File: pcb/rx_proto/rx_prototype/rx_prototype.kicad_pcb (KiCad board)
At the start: 10 copper layers, 50 parts, among them U1 nice_nano, U2 MPU-6500, U3 QMC5883P, U4 MCP6004, U5 MCP6004, U6 74HC4051

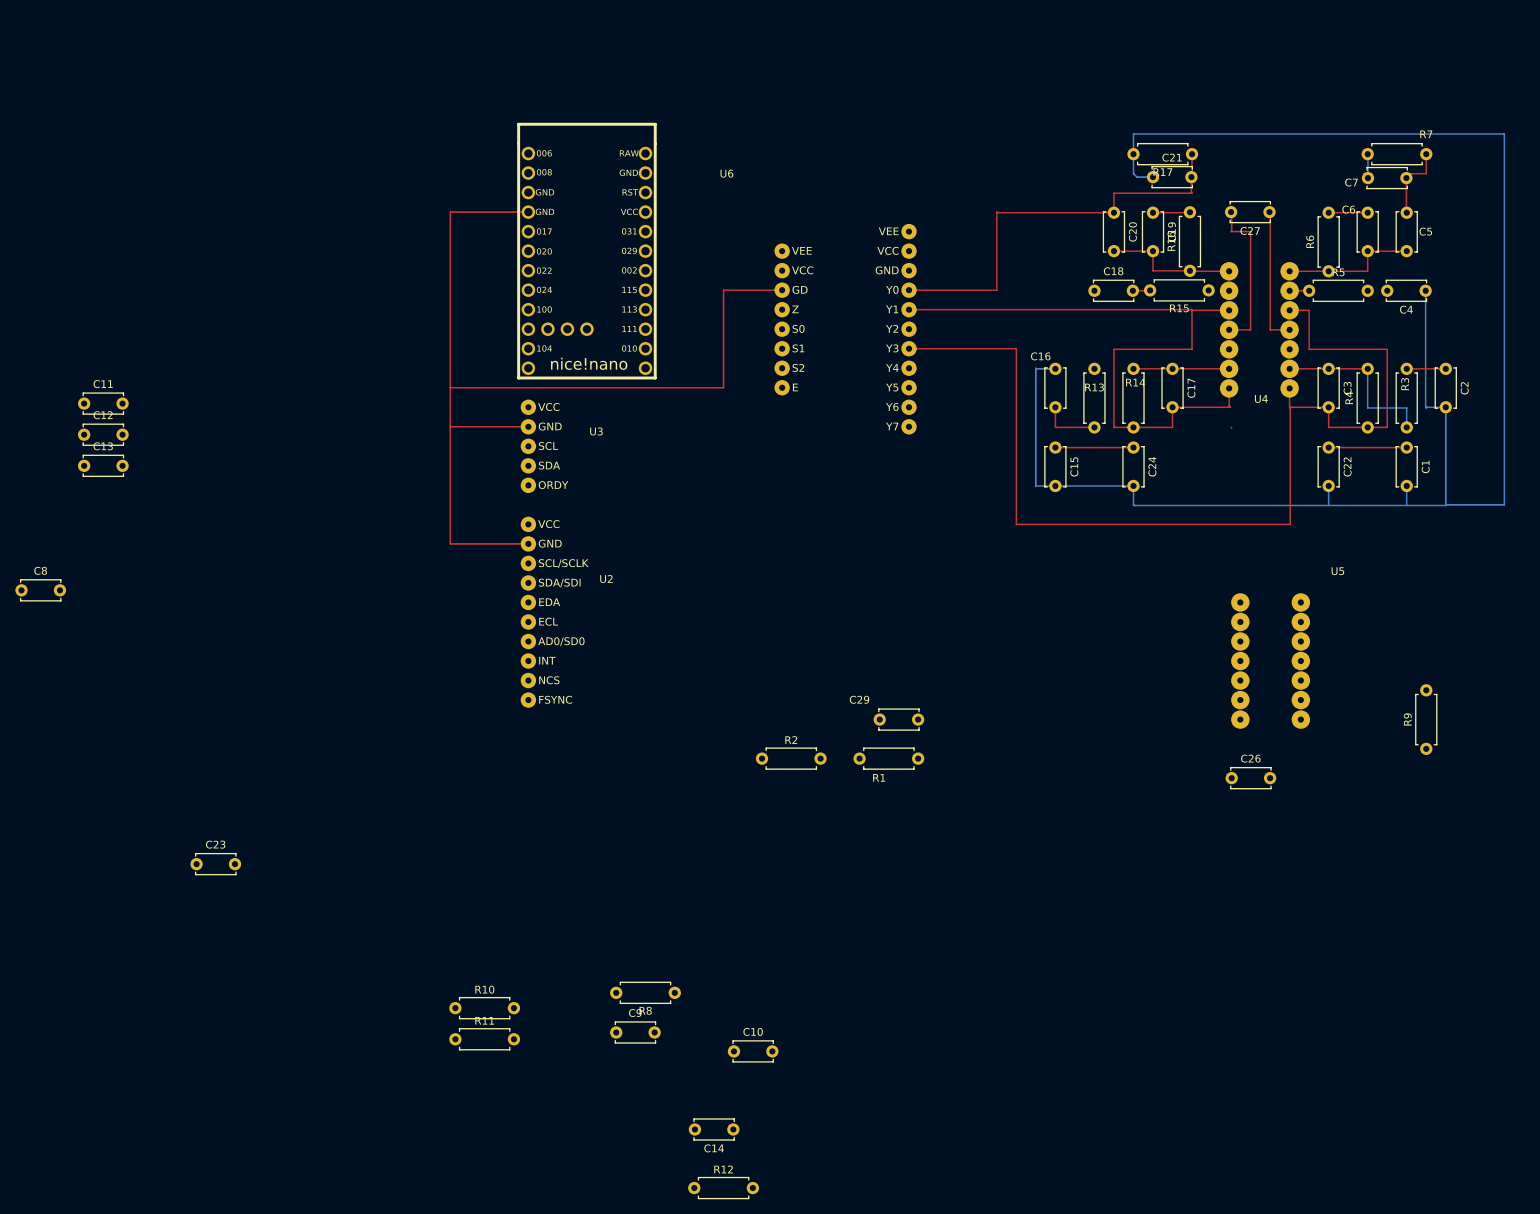
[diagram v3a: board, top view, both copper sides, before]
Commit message: Completed perboard prototype
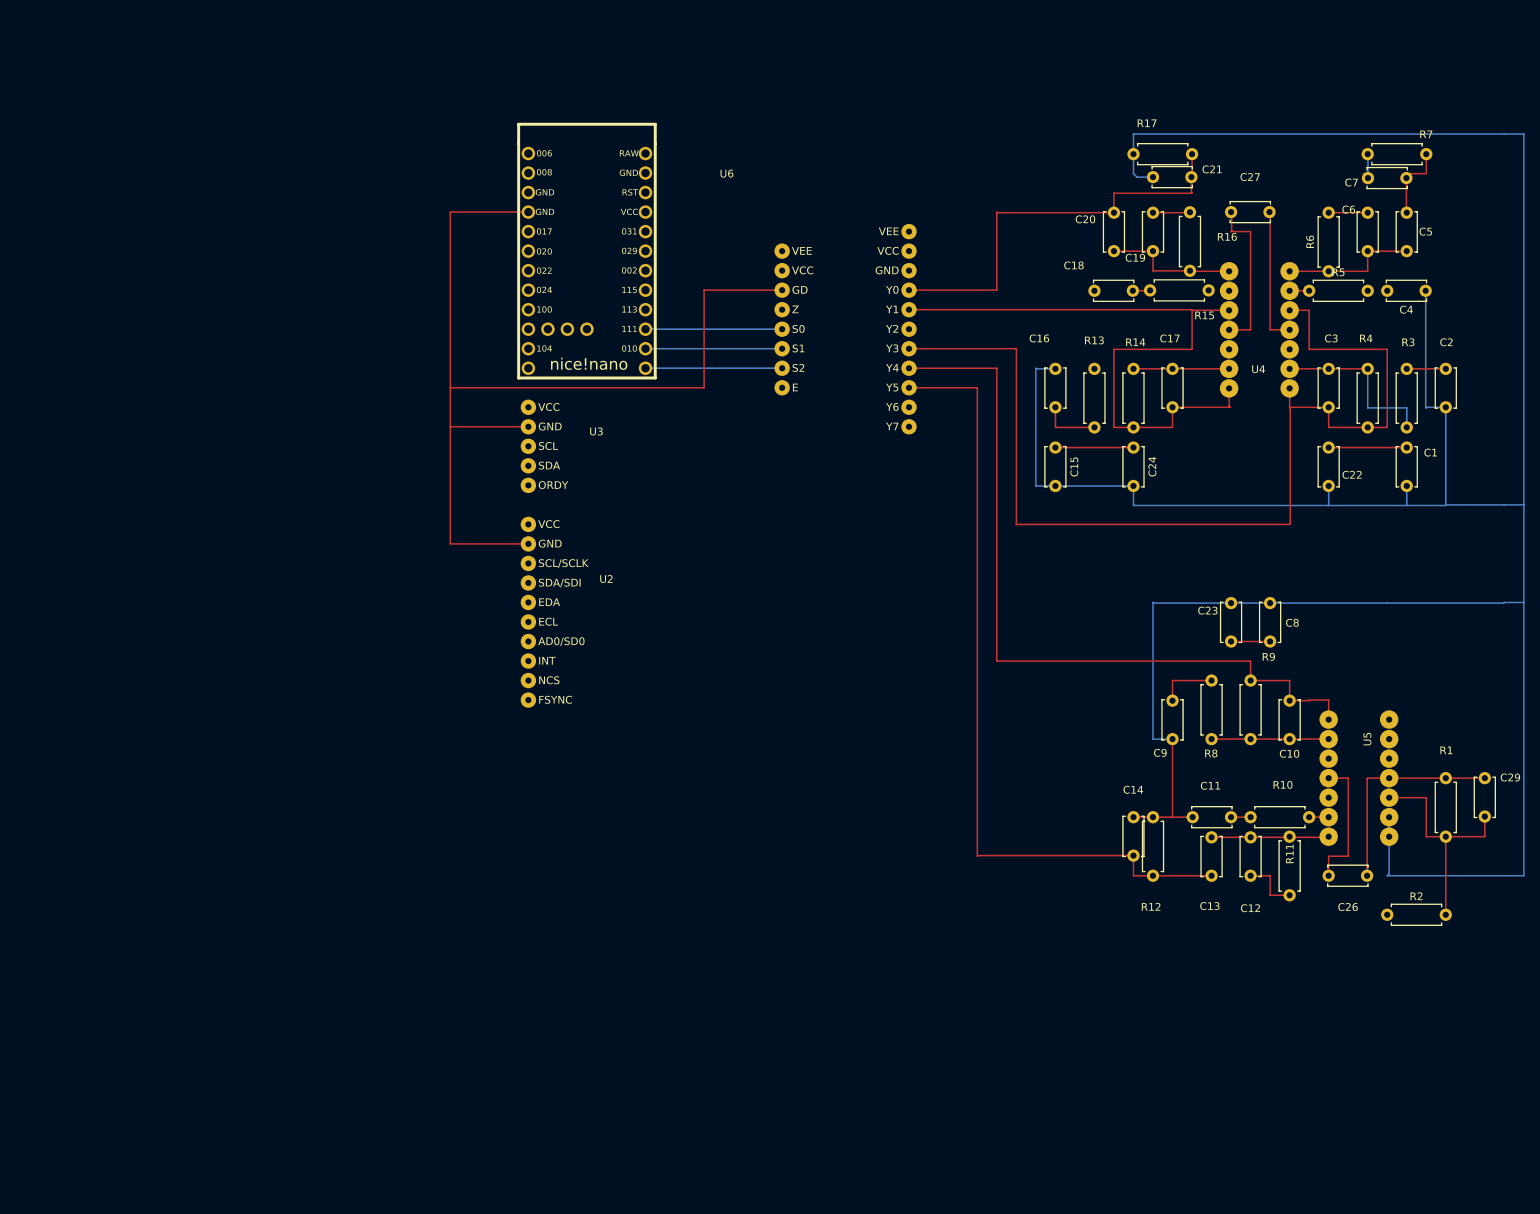
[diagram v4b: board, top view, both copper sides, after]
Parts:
- moved C8 162.6 mm to (223.5, 88.9), turned to 90 degrees
- moved C12 162.3 mm to (221.0, 119.4), turned to 90 degrees
- moved C13 156.1 mm to (215.9, 119.4), turned to 90 degrees
- moved C11 154.0 mm to (213.4, 111.8)
- moved C23 137.7 mm to (218.4, 88.9), turned to 90 degrees
- moved R10 113.8 mm to (228.6, 111.8), turned to 180 degrees
- moved R11 111.7 mm to (226.1, 114.3), turned to -90 degrees
- moved C9 84.3 mm to (210.8, 96.6), turned to -90 degrees
- moved R2 83.9 mm to (238.8, 124.5)
- moved C10 82.9 mm to (226.1, 101.6), turned to 90 degrees
- moved R8 77.3 mm to (215.9, 101.6), turned to 90 degrees
- moved R1 77.0 mm to (246.4, 114.3), turned to 90 degrees
- moved C29 74.1 mm to (251.5, 106.7), turned to -90 degrees
- moved R12 72.2 mm to (208.3, 119.4), turned to 90 degrees
- moved C14 66.1 mm to (205.7, 111.8), turned to -90 degrees
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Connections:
- C29 pad 2: Net-(U5D-+) -> Net-(U5C-+)
- R1 pad 1: Net-(U5D-+) -> Net-(U5C-+)
- R2 pad 2: Net-(U5D-+) -> Net-(U5C-+)
- U5 pad 10: /ADC_BUFFER -> Net-(U5C-+)
- U5 pad 12: Net-(U5D-+) -> /ADC_BUFFER
- U5 pad 13: /V_BIAS -> /ADC_0
- U5 pad 14: /V_BIAS -> /ADC_0
- U5 pad 8: /ADC_0 -> /V_BIAS
- U5 pad 9: /ADC_0 -> /V_BIAS
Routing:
- net /V_BIAS: track 240.8 -> 406.3 mm
- net /ADC_0: track 0.00 -> 157.9 mm
- net /ADC_BUFFER: track 0.00 -> 147.1 mm
- net GND: track 432.3 -> 544.1 mm
- net /V_OUT6: track 0.00 -> 103.0 mm
- net /V_OUT5: track 0.00 -> 100.4 mm
- net +3.3V: track 326.5 -> 364.6 mm
- net Net-(U5D-+): track 33.1 -> 0.00 mm
- net Net-(U5A-+): track 0.00 -> 33.1 mm
- net Net-(U5C-+): track 0.00 -> 30.3 mm
- net Net-(U5B--): track 0.00 -> 22.9 mm
- net /SELECT_2: track 0.00 -> 17.8 mm
- net /SELECT_1: track 0.00 -> 17.8 mm
- net /SELECT_0: track 0.00 -> 17.8 mm
- net Net-(C12-Pad2): track 0.00 -> 15.4 mm
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
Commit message: Compacted Perfboard
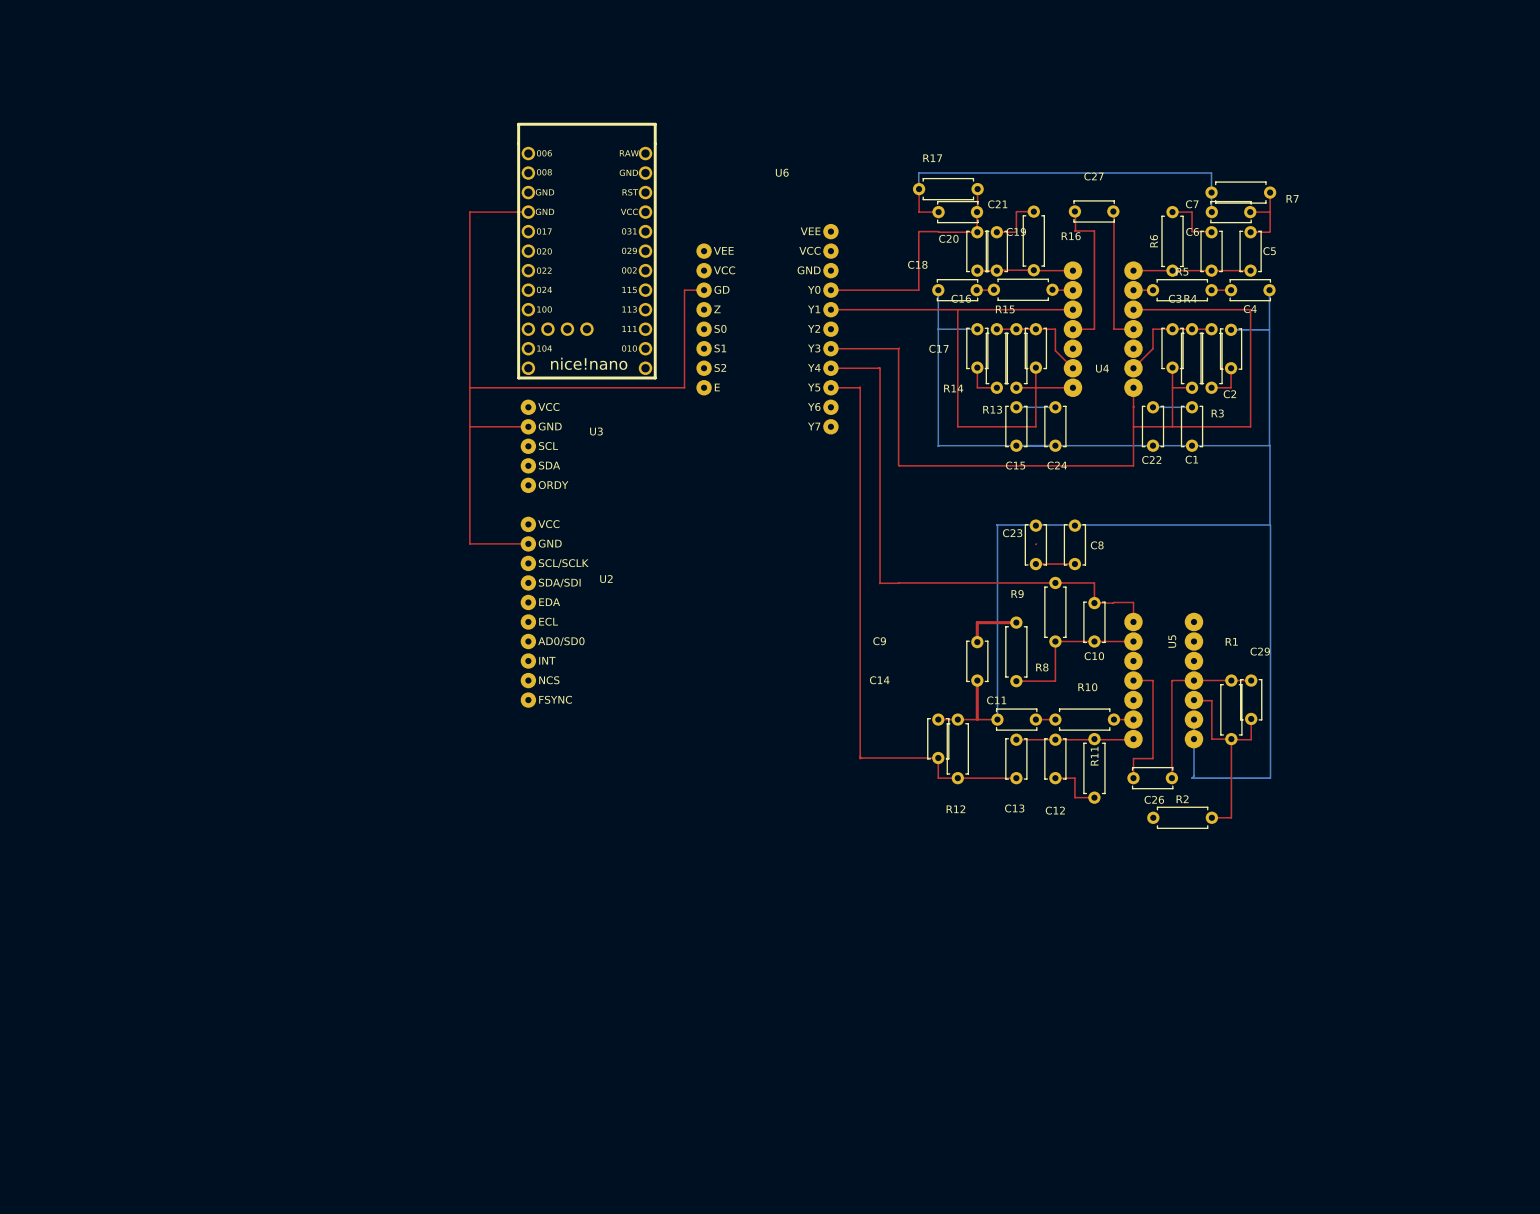
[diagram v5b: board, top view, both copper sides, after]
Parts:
- moved R2 33.0 mm to (208.3, 111.8)
- moved C29 32.9 mm to (221.1, 94.0)
- moved R1 30.7 mm to (218.5, 101.6)
- moved R3 28.4 mm to (215.9, 48.3), turned to -90 degrees
- moved C1 28.4 mm to (213.4, 58.4)
- moved C11 28.4 mm to (188.0, 99.1)
- moved C14 28.4 mm to (180.3, 99.1)
- moved R10 28.4 mm to (203.2, 99.1)
- moved R11 28.4 mm to (200.7, 101.6)
- moved C10 28.4 mm to (200.7, 88.9)
- moved C13 28.4 mm to (190.5, 106.7)
- moved R12 28.4 mm to (182.9, 106.7)
- moved R9 28.4 mm to (195.6, 81.3)
- moved U5 28.4 mm to (205.7, 83.8)
- moved C12 28.4 mm to (195.6, 106.7)
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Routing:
- net /V_BIAS: track 406.3 -> 295.0 mm
- net GND: track 544.1 -> 455.7 mm
- net +3.3V: track 364.6 -> 317.8 mm
- net /ADC_BUFFER: track 147.1 -> 114.0 mm
- net /ADC_0: track 157.9 -> 130.0 mm
- net /V_OUT5: track 100.4 -> 72.7 mm
- net /V_OUT6: track 103.0 -> 75.4 mm
- net /V_OUT2: track 54.7 -> 32.4 mm
- net Net-(U4D-+): track 32.5 -> 13.6 mm
- net /V_OUT1: track 87.4 -> 72.0 mm
- net /V_OUT4: track 110.3 -> 95.3 mm
- net /V_OUT3: track 133.5 -> 120.9 mm
- net Net-(U4A-+): track 25.0 -> 13.8 mm
- net /SELECT_2: track 17.8 -> 7.62 mm
- net /SELECT_1: track 17.8 -> 7.62 mm
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
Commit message: Backup Prototype
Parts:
- added L1: 0.7mH, Connector_PinHeader_2.54mm:PinHeader_1x02_P2.54mm_Vertical, F.Cu at (203.2, 61.0)
- added L3: 2mH, Connector_PinHeader_2.54mm:PinHeader_1x02_P2.54mm_Vertical, F.Cu at (203.2, 76.2)
- added L4: 2mH, Connector_PinHeader_2.54mm:PinHeader_1x02_P2.54mm_Vertical, F.Cu at (198.1, 61.0)
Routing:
- net /V_OUT5: track 72.7 -> 87.7 mm
- net Net-(U4A-+): track 13.8 -> 21.4 mm
- net Net-(U5A-+): track 30.4 -> 38.0 mm
- net GND: track 455.7 -> 450.1 mm
- net +3.3V: track 317.8 -> 312.5 mm
- net Net-(U4D-+): track 13.6 -> 18.7 mm
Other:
- board outline added: 121.9 x 101.6 mm

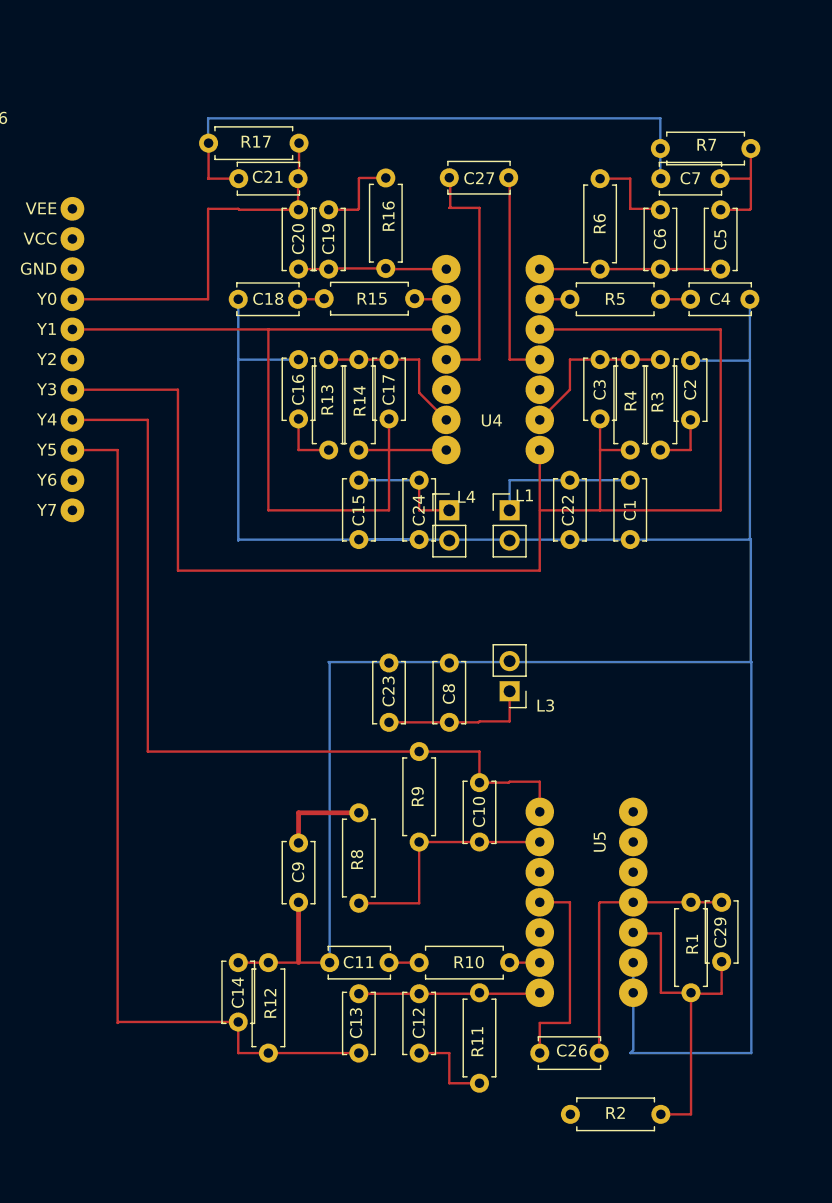
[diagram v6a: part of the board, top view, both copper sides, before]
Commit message: Update perfboard prototype front end
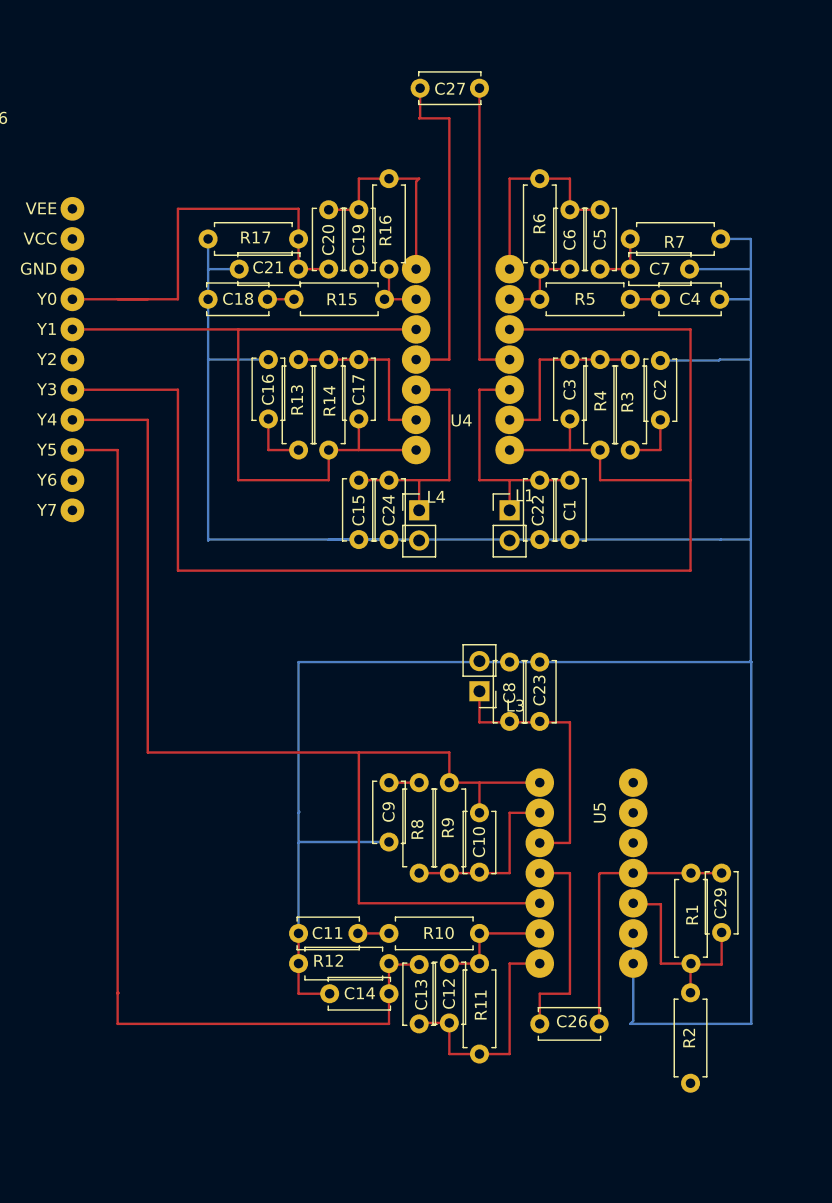
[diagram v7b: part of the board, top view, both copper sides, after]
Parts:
- moved C23 12.7 mm to (205.7, 78.7)
- moved R7 12.7 mm to (213.4, 38.1), turned to 0 degrees
- moved R12 12.7 mm to (193.0, 99.1), turned to 180 degrees
- moved C5 11.3 mm to (210.8, 40.6), turned to 90 degrees
- moved R2 10.5 mm to (218.4, 109.2), turned to 90 degrees
- moved C9 9.16 mm to (193.0, 83.9)
- moved R6 9.16 mm to (205.7, 33.0), turned to -90 degrees
- moved C6 9.11 mm to (208.3, 40.6), turned to 90 degrees
- moved C13 9.03 mm to (195.6, 99.2), turned to -90 degrees
- moved C14 8.13 mm to (188.0, 101.7), turned to 0 degrees
- moved R17 8.07 mm to (185.4, 38.1)
- moved C7 8.00 mm to (218.4, 40.6), turned to 180 degrees
- moved C12 7.96 mm to (198.1, 99.1), turned to -90 degrees
- moved C27 7.93 mm to (200.7, 25.4)
- moved C21 7.62 mm to (180.4, 40.6)
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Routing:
- net /V_BIAS: track 295.0 -> 262.6 mm
- net /V_OUT4: track 95.3 -> 77.4 mm
- net Net-(U4C--): track 23.5 -> 5.78 mm
- net Net-(U4B--): track 22.9 -> 7.63 mm
- net Net-(U5A-+): track 38.0 -> 22.9 mm
- net /V_OUT5: track 87.7 -> 100.4 mm
- net Net-(U5B--): track 22.9 -> 10.3 mm
- net Net-(U5C-+): track 28.0 -> 17.7 mm
- net /V_OUT1: track 72.0 -> 61.8 mm
- net GND: track 450.1 -> 441.8 mm
- net /V_OUT6: track 75.0 -> 82.8 mm
- net /SDA: track 53.3 -> 61.0 mm
- net /SCK: track 55.9 -> 48.3 mm
- net Net-(C19-Pad2): track 12.5 -> 18.0 mm
- net +3.3V: track 312.5 -> 317.7 mm
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
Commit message: Created rx board for order
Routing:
- net /SELECT_1: track 7.62 -> 0.00 mm
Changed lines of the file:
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@@
-	)
-	(segment
-		(start 142.24 50.8)
-		(end 149.86 50.8)
-		(width 0.2)
-		(layer "In1.Cu")
-		(net "/SELECT_1")
 	)
 	(segment
